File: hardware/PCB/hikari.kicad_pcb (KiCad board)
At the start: 2 copper layers, 65 x 65 mm, 58 parts, among them CN1 USB-C, CN2 1x3, IC1 PAM2804AAB010, IC2 PAM2804AAB010, IC3 PAM2804AAB010, IC4 PAM2804AAB010, IC5 ESP-12F, IC6 CH340G, IC7 AP2112K-3.3TRG1, SW1 LS12W3-T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

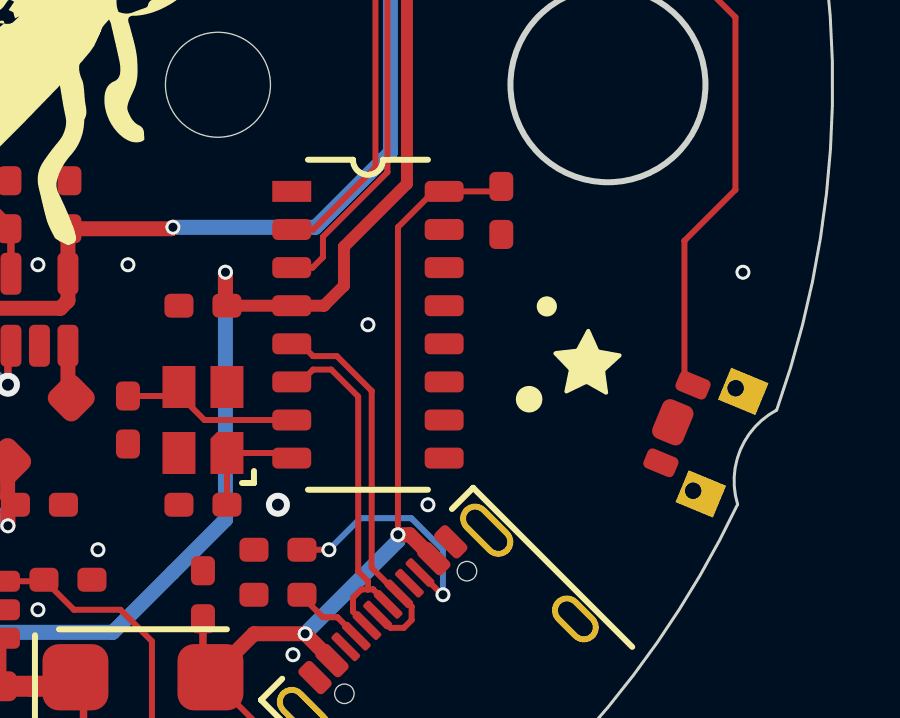
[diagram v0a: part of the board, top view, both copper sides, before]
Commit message: fixed the pcb being powered via ch340g
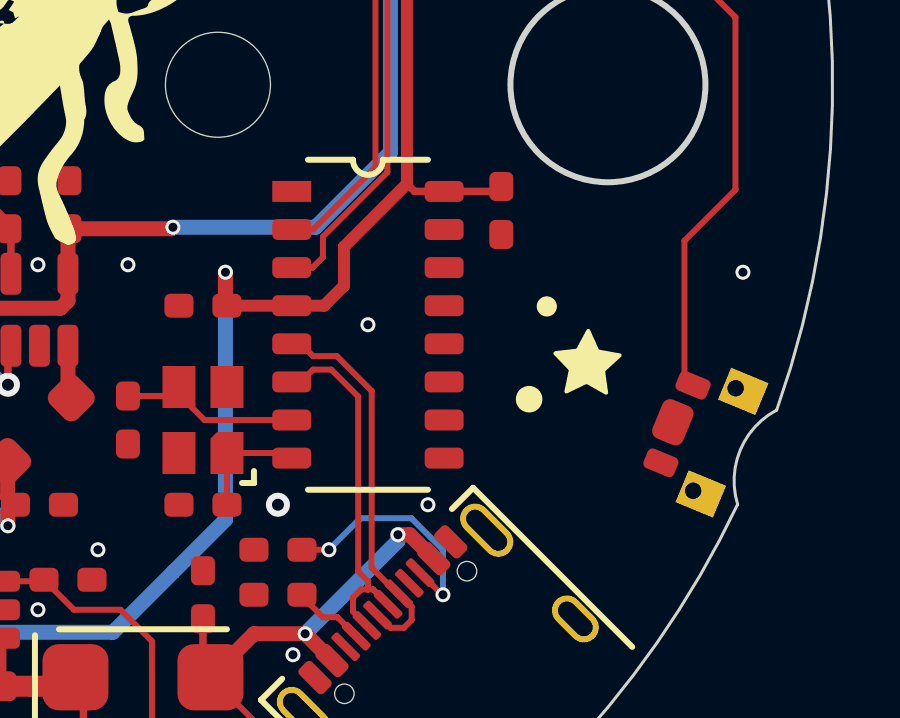
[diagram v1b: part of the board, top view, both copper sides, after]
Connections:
- C14 pad 1: /Power supply/V_USB -> 3V3
- IC6 pad 16: /Power supply/V_USB -> 3V3
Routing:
- net /Power supply/V_USB: track 46.8 -> 32.5 mm
- net 3V3: track 114.3 -> 118.0 mm
